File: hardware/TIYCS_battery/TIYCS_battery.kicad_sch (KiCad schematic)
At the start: 23 parts, among them J1 Barrel_Jack_Switch, J2 External Jack, J3 pinHeaders, U1 4S_BMS, U2 4_18650, U3 XL4015

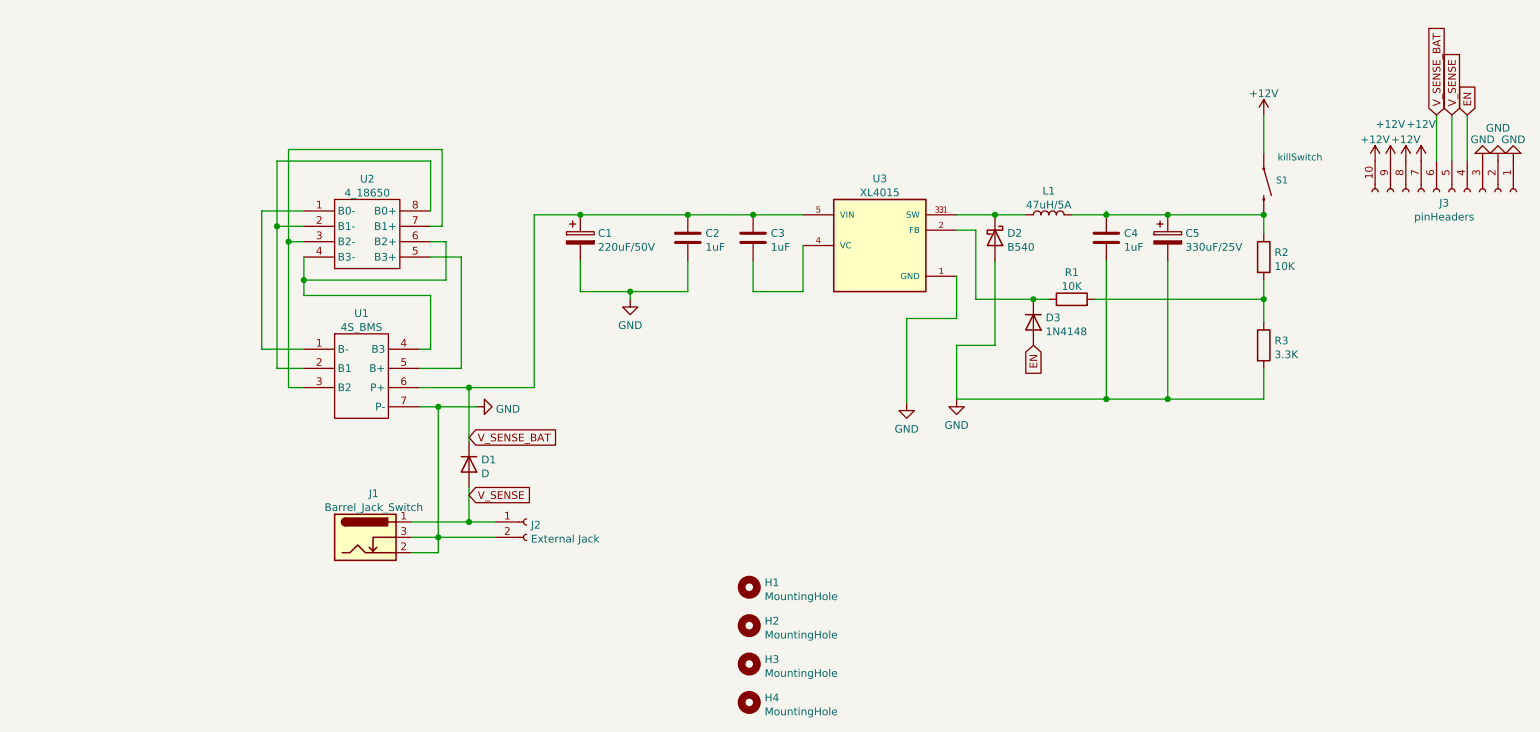
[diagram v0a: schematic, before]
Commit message: Moved switch, cleared PCB file, changed voltage divider
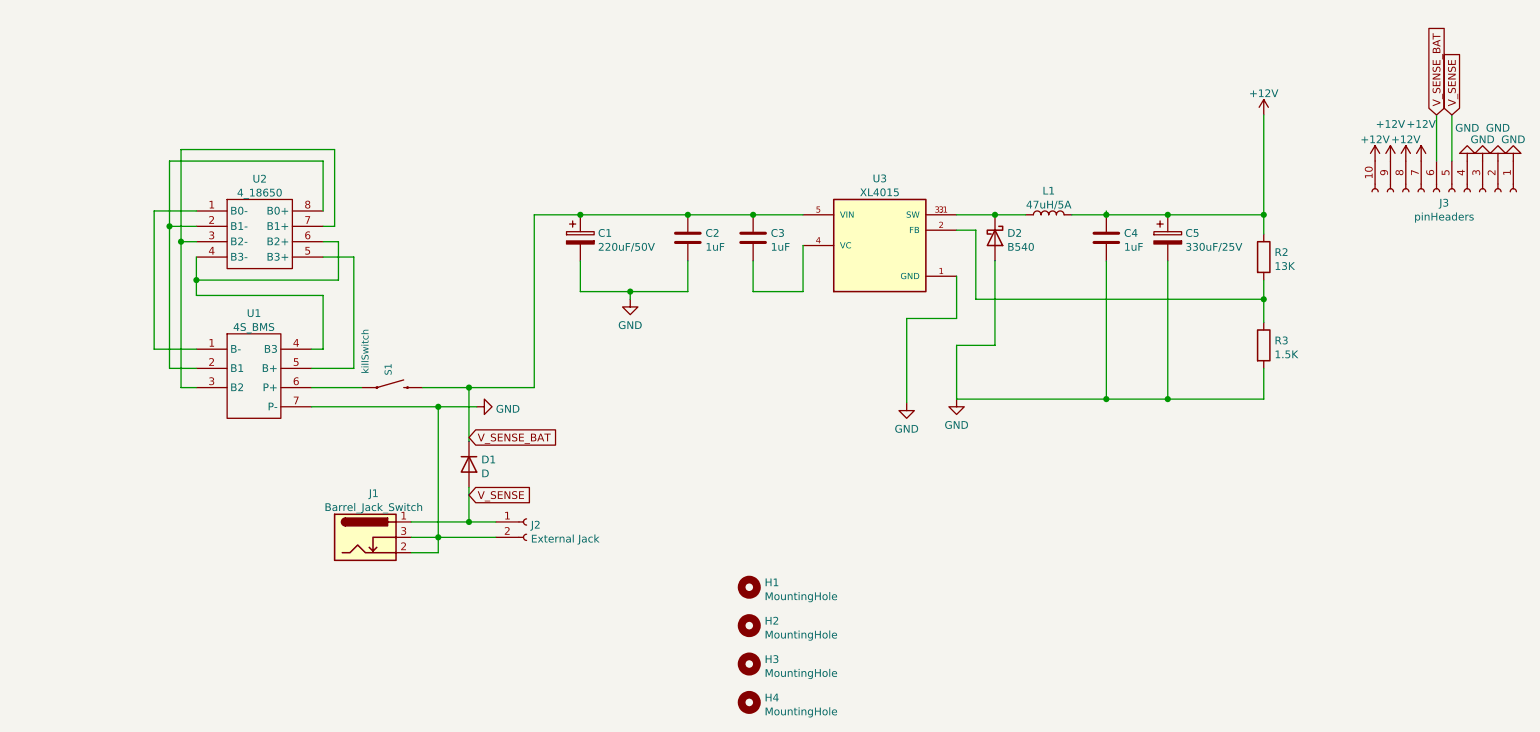
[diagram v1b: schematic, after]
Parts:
- removed D3: 1N4148, Diode_SMD:D_SOD-323F, symbol Device:D
- removed R1: 10K, Resistors:0805, symbol Device:R
- R2: value 10K -> 13K
- R3: value 3.3K -> 1.5K
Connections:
- net EN is gone; now on net GND: J3.4 (Pin_4)
- net +12V: now also C4.1, C5.1, L1.2, R2.1; no longer S1.1
- net V_SENSE_BAT: now also S1.2; no longer U1.6 (P+)
- net at R2.2, R3.1: now also U3.2 (FB)
- new net: S1.1, U1.6 (P+)
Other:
- moved on the sheet: S1, U1, U2

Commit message: Start with new LDO, fuse
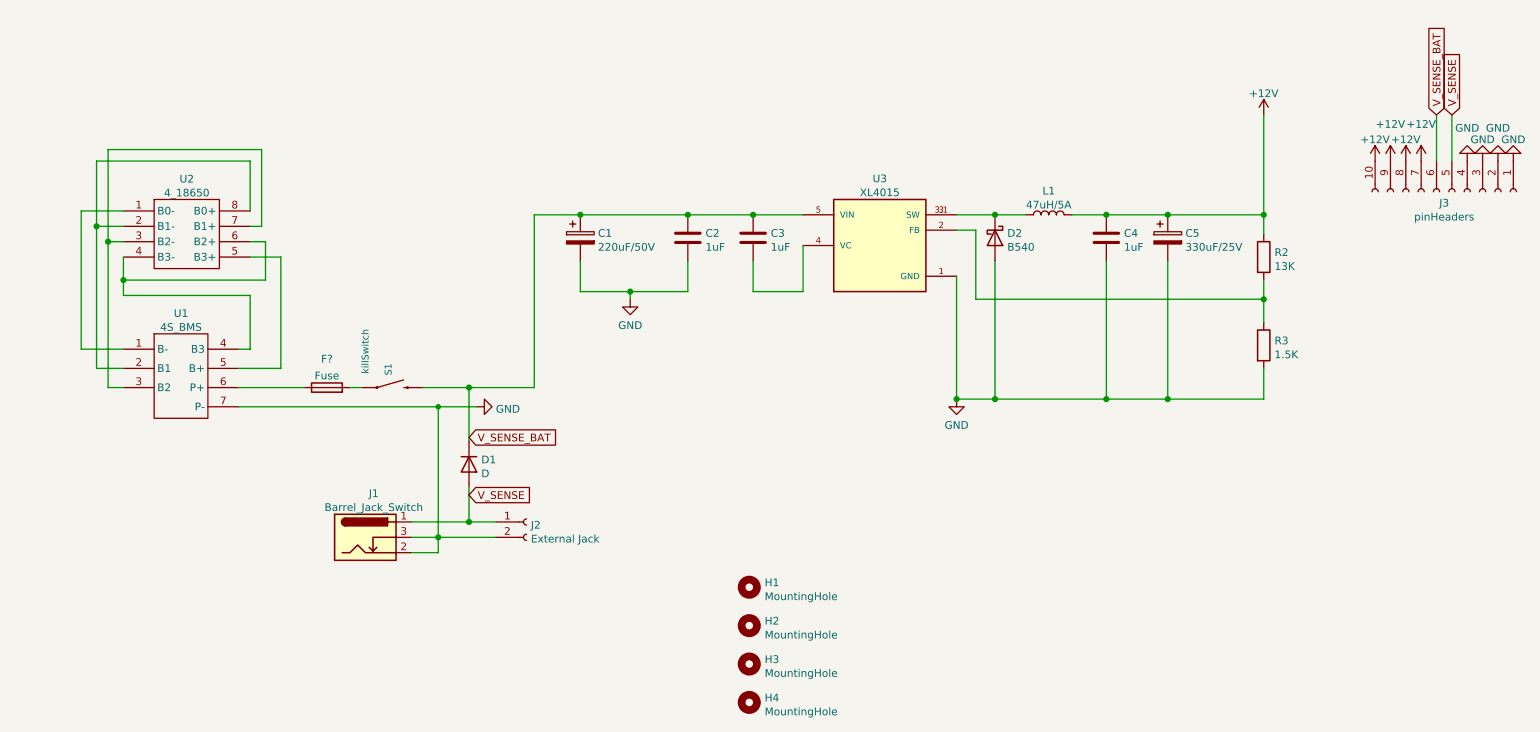
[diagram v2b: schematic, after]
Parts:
- added F?: Fuse, symbol Device:Fuse
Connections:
- net at U1.6 (P+): now also F?.1; no longer S1.1
- new net: F?.2, S1.1
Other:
- moved on the sheet: U1, U2

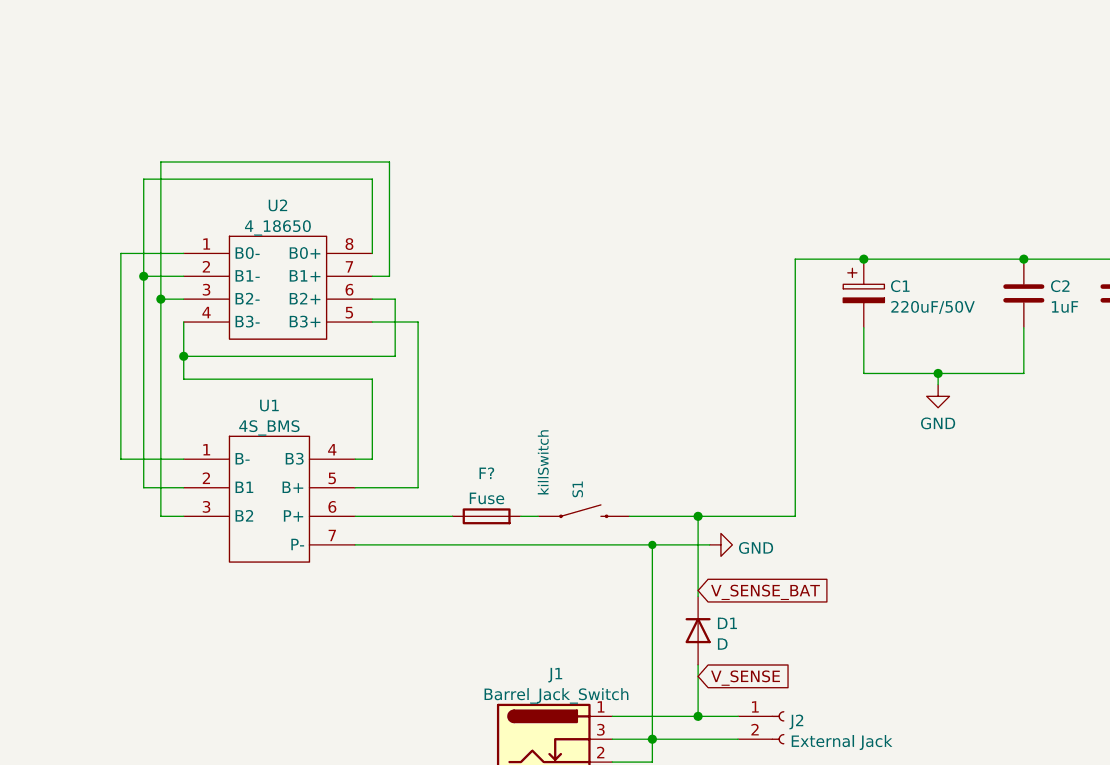
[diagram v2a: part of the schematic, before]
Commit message: First version of ledPanel: board outline + pins
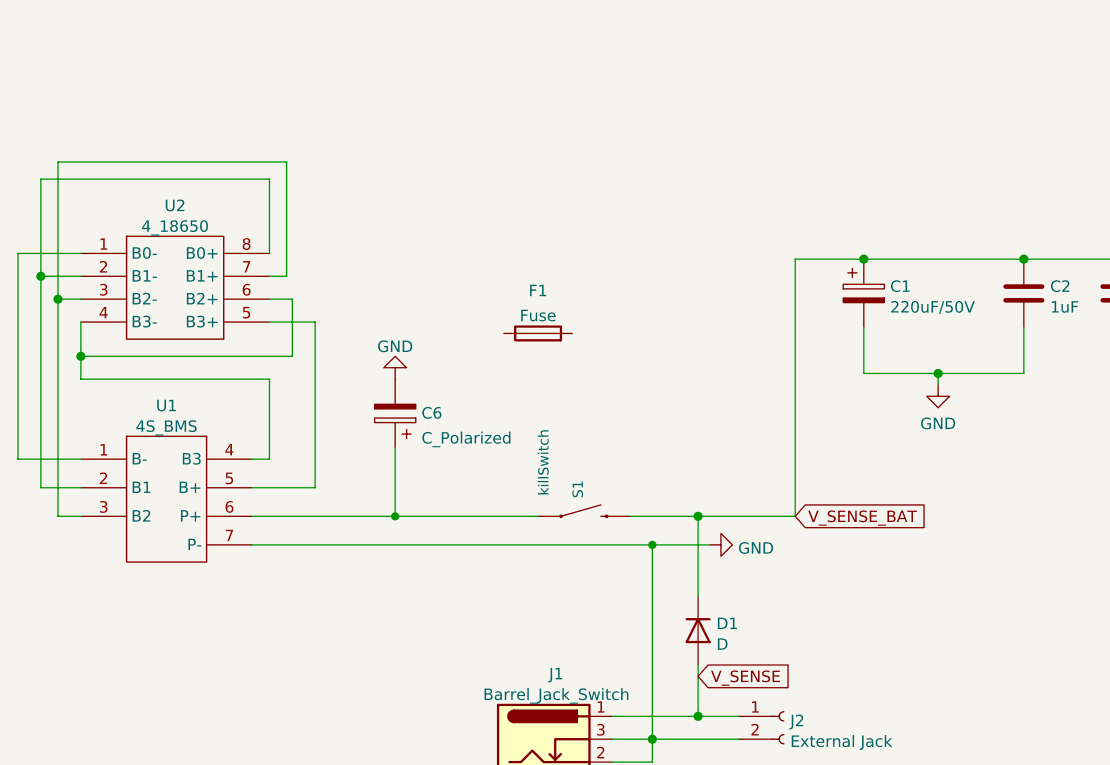
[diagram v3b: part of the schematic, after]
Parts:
- added C6: C_Polarized, Capacitor_THT:CP_Radial_D12.5mm_P5.00mm, symbol Device:C_Polarized
- F1: renamed from F?; footprint (none) -> Fuse:Fuse_2920_7451Metric
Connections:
- net GND: now also C6.2
- net at U1.6 (P+): now also S1.1, C6.1; no longer F1.1
- net at F1.2: no longer S1.1
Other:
- moved on the sheet: F1, U1, U2

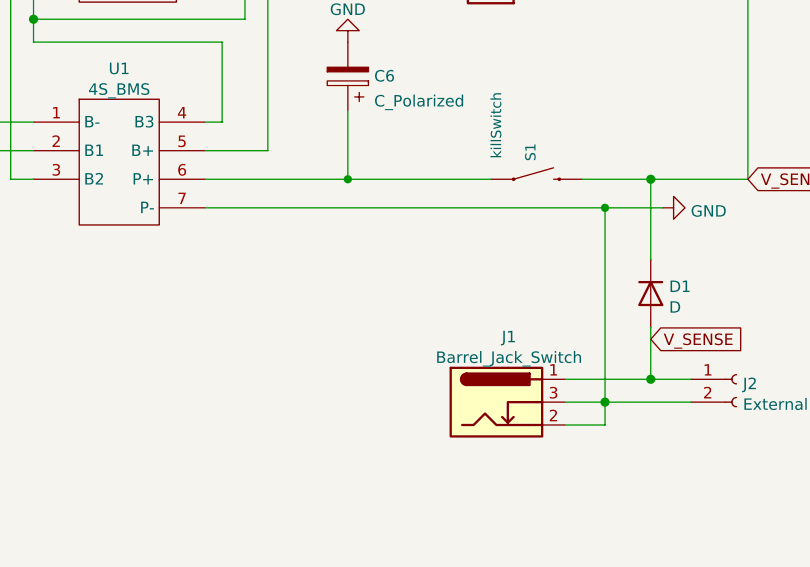
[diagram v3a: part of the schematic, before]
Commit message: Added XT60 conn to battery board
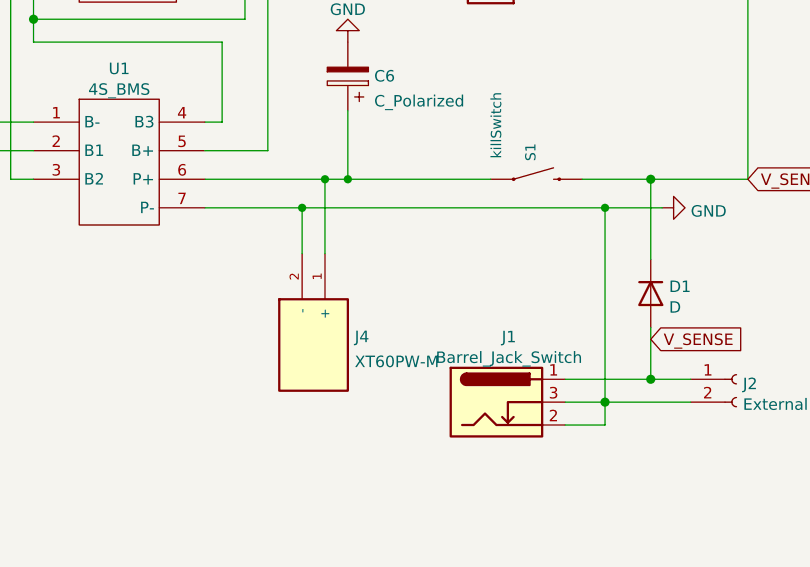
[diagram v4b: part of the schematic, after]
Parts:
- added J4: XT60PW-M, XT60PW-M:AMASS_XT60PW-M, symbol XT60PW-M:XT60PW-M
- R3: footprint Resistors:0805 -> Resistor_SMD:R_0805_2012Metric
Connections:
- net GND: now also J4.2 (-)
- net at C6.1, S1.1, U1.6 (P+): now also J4.1 (+)
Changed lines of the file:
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@@
   (junction (at 200.025 76.835) (diameter 1.016) (color 0 0 0 0)
   )
+  (junction (at 48.26 74.93) (diameter 0) (color 0 0 0 0)
+  )
   (junction (at 79.375 99.695) (diameter 1.016) (color 0 0 0 0)
   )
@@
   )
   (junction (at 120.65 46.355) (diameter 1.016) (color 0 0 0 0)
+  )
+  (junction (at 45.72 78.105) (diameter 0) (color 0 0 0 0)
   )
   (junction (at 189.865 46.355) (diameter 1.016) (color 0 0 0 0)
@@
     (stroke (width 0) (type solid) (color 0 0 0 0))
   )
+  (wire (pts (xy 48.26 74.93) (xy 50.8 74.93))
+    (stroke (width 0) (type solid) (color 0 0 0 0))
+  )
   (wire (pts (xy 200.025 46.355) (xy 215.9 46.355))
     (stroke (width 0) (type solid) (color 0 0 0 0))
@@
     (stroke (width 0) (type solid) (color 0 0 0 0))
   )
-  (wire (pts (xy 34.925 78.105) (xy 79.375 78.105))
+  (wire (pts (xy 34.925 78.105) (xy 45.72 78.105))
     (stroke (width 0) (type default) (color 0 0 0 0))
   )
@@
   (wire (pts (xy 244.475 29.845) (xy 244.475 37.465))
     (stroke (width 0) (type solid) (color 0 0 0 0))
+  )
+  (wire (pts (xy 48.26 74.93) (xy 48.26 83.185))
+    (stroke (width 0) (type default) (color 0 0 0 0))
   )
   (wire (pts (xy 165.1 48.895) (xy 168.275 48.895))
@@
     (stroke (width 0) (type solid) (color 0 0 0 0))
   )
-  (wire (pts (xy 34.925 74.93) (xy 50.8 74.93))
+  (wire (pts (xy 34.925 74.93) (xy 48.26 74.93))
     (stroke (width 0) (type solid) (color 0 0 0 0))
   )
@@
     (stroke (width 0) (type solid) (color 0 0 0 0))
   )
+  (wire (pts (xy 45.72 78.105) (xy 45.72 83.185))
+    (stroke (width 0) (type default) (color 0 0 0 0))
+  )
   (wire (pts (xy 131.445 59.055) (xy 139.7 59.055))
     (stroke (width 0) (type solid) (color 0 0 0 0))
@@
   (wire (pts (xy 200.025 53.975) (xy 200.025 76.835))
     (stroke (width 0) (type solid) (color 0 0 0 0))
+  )
+  (wire (pts (xy 45.72 78.105) (xy 79.375 78.105))
+    (stroke (width 0) (type default) (color 0 0 0 0))
   )
   (wire (pts (xy 74.93 102.235) (xy 79.375 102.235))
@@
     (pin "8")
   )
+  (symbol (lib_id "XT60PW-M:XT60PW-M") (at 45.72 93.345 270) (unit 1)
+    (in_bom yes) (on_board yes) (fields_autoplaced)
+    (property "Reference" "J4" (id 0) (at 51.562 92.4365 90)
+      (effects (font (size 1.27 1.27)) (justify left))
+    )
+    (property "Value" "XT60PW-M" (id 1) (at 51.562 95.2116 90)
+      (effects (font (size 1.27 1.27)) (justify left))
+    )
+    (property "Footprint" "XT60PW-M:AMASS_XT60PW-M" (id 2) (at 45.72 93.345 0)
+      (effects (font (size 1.27 1.27)) (justify left bottom) hide)
+    )
+    (property "Datasheet" "" (id 3) (at 45.72 93.345 0)
+      (effects (font (size 1.27 1.27)) (justify left bottom) hide)
+    )
+    (property "MAXIMUM_PACKAGE_HEIGHT" "8.4 mm" (id 4) (at 45.72 93.345 0)
+      (effects (font (size 1.27 1.27)) (justify left bottom) hide)
+    )
+    (property "MANUFACTURER" "AMASS" (id 5) (at 45.72 93.345 0)
+      (effects (font (size 1.27 1.27)) (justify left bottom) hide)
+    )
+    (property "PARTREV" "V1.2" (id 6) (at 45.72 93.345 0)
+      (effects (font (size 1.27 1.27)) (justify left bottom) hide)
+    )
+    (property "STANDARD" "Manufacturer recommendations" (id 7) (at 45.72 93.345 0)
+      (effects (font (size 1.27 1.27)) (justify left bottom) hide)
+    )
+    (property "JLCPCB" "C98732" (id 8) (at 45.72 93.345 90)
+      (effects (font (size 1.27 1.27)) hide)
+    )
+    (pin "1")
+    (pin "2")
+  )
   (symbol (lib_id "Device:R") (at 215.9 53.34 0) (unit 1)
     (in_bom yes) (on_board yes) (fields_autoplaced)
@@
       (effects (font (size 1.27 1.27)) (justify left))
     )
-    (property "Footprint" "Resistors:0805" (id 2) (at 214.122 67.945 90)
+    (property "Footprint" "Resistor_SMD:R_0805_2012Metric" (id 2) (at 214.122 67.945 90)
       (effects (font (size 1.27 1.27)) hide)
     )
@@
       (reference "J3") (unit 1) (value "pinHeaders") (footprint "Connector_PinHeader_2.54mm:PinHeader_1x10_P2.54mm_Vertical")
     )
+    (path "/47994eea-42d7-42df-9b92-2247790f72b8"
+      (reference "J4") (unit 1) (value "XT60PW-M") (footprint "XT60PW-M:AMASS_XT60PW-M")
+    )
     (path "/7f1fc9df-29e3-447b-97b1-6044afd23fc4"
       (reference "L1") (unit 1) (value "47uH/5A") (footprint "jildertTest:YSPI1365")
@@
     )
     (path "/a316ea80-320a-4bdd-ba40-eba76bb5a2d4"
-      (reference "R3") (unit 1) (value "1.5K") (footprint "Resistors:0805")
+      (reference "R3") (unit 1) (value "1.5K") (footprint "Resistor_SMD:R_0805_2012Metric")
     )
     (path "/8fa07fb6-923d-4a90-8c74-9bf4c07e28bd"
